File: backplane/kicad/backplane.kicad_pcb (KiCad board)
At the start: 4 copper layers, 141.2 x 81.1 mm, 6 parts, among them J1 weactstm32h7xx, J2 pcie_98, J3 pcie_98, J4 pcie_98, J5 pcie_98, J6 pcie_98

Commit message: Work in progress. Backlane kicad.
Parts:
- added H1: MountingHole, MountingHole:MountingHole_3.2mm_M3_Pad_Via, F.Cu at (84.0, 74.0)
- added H2: MountingHole, MountingHole:MountingHole_3.2mm_M3_Pad_Via, F.Cu at (145.0, 133.0)
- added H3: MountingHole, MountingHole:MountingHole_3.2mm_M3_Pad_Via, F.Cu at (84.0, 133.0)
- added H4: MountingHole, MountingHole:MountingHole_3.2mm_M3_Pad_Via, F.Cu at (217.0, 74.0)
- added H5: MountingHole, MountingHole:MountingHole_3.2mm_M3_Pad_Via, F.Cu at (145.0, 74.0)
- added H6: MountingHole, MountingHole:MountingHole_3.2mm_M3_Pad_Via, F.Cu at (217.0, 133.0)
- added J2: Conn_01x05_Pin, backplane:JST_XH_B5B-XH-AM_1x05_P2.50mm_Vertical, F.Cu at (84.0, 100.0)
- added S1: pcie_98, backplane:pcie_98_socket, F.Cu at (100.0, 90.0)
- added S7: pcie_98, backplane:pcie_98_socket, F.Cu at (208.0, 90.0)
- J1: value weactstm32h7xx -> Conn_01x02_Pin; footprint main_board:weact_stm32fh750 -> backplane:JST_XH_B2B-XH-AM_1x02_P2.50mm_Vertical
- S2: renamed from J2; footprint main_board:pcie_98_socket -> backplane:pcie_98_socket
- S3: renamed from J3; footprint main_board:pcie_98_socket -> backplane:pcie_98_socket
- S4: renamed from J4; footprint main_board:pcie_98_socket -> backplane:pcie_98_socket
- S5: renamed from J5; footprint main_board:pcie_98_socket -> backplane:pcie_98_socket
- S6: renamed from J6; footprint main_board:pcie_98_socket -> backplane:pcie_98_socket
- moved S6 77.5 mm to (190.0, 90.0)
- moved S5 76.4 mm to (172.0, 90.0)
- moved S4 74.7 mm to (154.0, 90.0)
- moved S3 72.9 mm to (136.0, 90.0)
- moved S2 70.1 mm to (118.0, 90.0)
- moved J1 50.6 mm to (84.0, 87.0), turned to -90 degrees
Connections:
- J1 pad 1: /GND -> unconnected-(J1-Pin_1-Pad1)
- J1 pad 2: /5V -> unconnected-(J1-Pin_2-Pad2)
- S2 pad A1: unconnected-(J2-Pin_a1-PadA1) -> /A1
- S2 pad A10: unconnected-(J2-Pin_a10-PadA10) -> /A10
- S2 pad A11: unconnected-(J2-Pin_A11-PadA11) -> /A11
- S2 pad A12: unconnected-(J2-Pin_a12-PadA12) -> /A12
- S2 pad A13: unconnected-(J2-Pin_a13-PadA13) -> /A13
- S2 pad A14: unconnected-(J2-Pin_a14-PadA14) -> /A14
- S2 pad A15: unconnected-(J2-Pin_a15-PadA15) -> /A15
- S2 pad A16: unconnected-(J2-Pin_a16-PadA16) -> /A16
- S2 pad A17: unconnected-(J2-Pin_a17-PadA17) -> /A17
- S2 pad A18: unconnected-(J2-Pin_a18-PadA18) -> /A18
- S2 pad A19: unconnected-(J2-Pin_a19-PadA19) -> /A19
- S2 pad A2: unconnected-(J2-Pin_a2-PadA2) -> /A2
- S2 pad A21: unconnected-(J2-Pin_a21-PadA21) -> /A21
- S2 pad A22: unconnected-(J2-Pin_a22-PadA22) -> /A22
- S2 pad A23: unconnected-(J2-Pin_a23-PadA23) -> /A23
- S2 pad A24: unconnected-(J2-Pin_a24-PadA24) -> /A24
- S2 pad A25: unconnected-(J2-Pin_a25-PadA25) -> /A25
- S2 pad A26: unconnected-(J2-Pin_a26-PadA26) -> /A26
- S2 pad A27: unconnected-(J2-Pin_a27-PadA27) -> /A27
- S2 pad A28: unconnected-(J2-Pin_a28-PadA28) -> /A28
- S2 pad A29: unconnected-(J2-Pin_a29-PadA29) -> /A29
- S2 pad A3: unconnected-(J2-Pin_a3-PadA3) -> /A3
- S2 pad A30: unconnected-(J2-Pin_a30-PadA30) -> /A30
- S2 pad A31: unconnected-(J2-Pin_a31-PadA31) -> /A31
- S2 pad A32: unconnected-(J2-Pin_a32-PadA32) -> /A32
- S2 pad A33: unconnected-(J2-Pin_a33-PadA33) -> /A33
- S2 pad A34: unconnected-(J2-Pin_a34-PadA34) -> /A34
- S2 pad A35: unconnected-(J2-Pin_a35-PadA35) -> /A35
- S2 pad A36: unconnected-(J2-Pin_a36-PadA36) -> /A36
- S2 pad A37: unconnected-(J2-Pin_a37-PadA37) -> /A37
- S2 pad A38: unconnected-(J2-Pin_a38-PadA38) -> /A38
- S2 pad A39: unconnected-(J2-Pin_a39-PadA39) -> /A39
- S2 pad A4: unconnected-(J2-Pin_a4-PadA4) -> /A4
- S2 pad A40: unconnected-(J2-Pin_a40-PadA40) -> /A40
- S2 pad A41: unconnected-(J2-Pin_a41-PadA41) -> /A41
- S2 pad A42: unconnected-(J2-Pin_a42-PadA42) -> /A42
- S2 pad A43: unconnected-(J2-Pin_a43-PadA43) -> /A43
- S2 pad A44: unconnected-(J2-Pin_a44-PadA44) -> /A44
- S2 pad A45: unconnected-(J2-Pin_a45-PadA45) -> /A45
- S2 pad A46: unconnected-(J2-Pin_a46-PadA46) -> /A46
- S2 pad A47: unconnected-(J2-Pin_a47-PadA47) -> /A47
- S2 pad A48: unconnected-(J2-Pin_a48-PadA48) -> /A48
- S2 pad A49: unconnected-(J2-Pin_a49-PadA49) -> /A49
- S2 pad A5: unconnected-(J2-Pin_a5-PadA5) -> /A5
- S2 pad A6: unconnected-(J2-Pin_a6-PadA6) -> /A6
- S2 pad A7: unconnected-(J2-Pin_a7-PadA7) -> /A7
- S2 pad A8: unconnected-(J2-Pin_a8-PadA8) -> /A8
- S2 pad A9: unconnected-(J2-Pin_a9-PadA9) -> /A9
- S2 pad B1: unconnected-(J2-Pin_b1-PadB1) -> /B1
- S2 pad B10: unconnected-(J2-Pin_b10-PadB10) -> /B10
- S2 pad B11: unconnected-(J2-Pin_b11-PadB11) -> /B11
- S2 pad B12: unconnected-(J2-Pin_b12-PadB12) -> /B12
- S2 pad B13: unconnected-(J2-Pin_b13-PadB13) -> /B13
- S2 pad B14: unconnected-(J2-Pin_b14-PadB14) -> /B14
- S2 pad B15: unconnected-(J2-Pin_b15-PadB15) -> /B15
- S2 pad B16: unconnected-(J2-Pin_b16-PadB16) -> /B16
- S2 pad B17: unconnected-(J2-Pin_b17-PadB17) -> /B17
- S2 pad B18: unconnected-(J2-Pin_b18-PadB18) -> /B18
- S2 pad B19: unconnected-(J2-Pin_b19-PadB19) -> /B19
- S2 pad B2: unconnected-(J2-Pin_b2-PadB2) -> /B2
- S2 pad B20: unconnected-(J2-Pin_b20-PadB20) -> /B20
- S2 pad B21: unconnected-(J2-Pin_b21-PadB21) -> /B21
- S2 pad B22: unconnected-(J2-Pin_b22-PadB22) -> /B22
- S2 pad B23: unconnected-(J2-Pin_b23-PadB23) -> /B23
- S2 pad B3: unconnected-(J2-Pin_b3-PadB3) -> /B3
- S2 pad B4: unconnected-(J2-Pin_b4-PadB4) -> /B4
- S2 pad B5: unconnected-(J2-Pin_b5-PadB5) -> /B5
- S2 pad B6: unconnected-(J2-Pin_b6-PadB6) -> /B6
- S2 pad B7: unconnected-(J2-Pin_b7-PadB7) -> /B7
- S2 pad B8: unconnected-(J2-Pin_b8-PadB8) -> /B8
- S2 pad B9: unconnected-(J2-Pin_b9-PadB9) -> /B9
- S3 pad A1: unconnected-(J3-Pin_a1-PadA1) -> /A1
- S3 pad A10: unconnected-(J3-Pin_a10-PadA10) -> /A10
- S3 pad A11: unconnected-(J3-Pin_A11-PadA11) -> /A11
- S3 pad A12: unconnected-(J3-Pin_a12-PadA12) -> /A12
- S3 pad A13: unconnected-(J3-Pin_a13-PadA13) -> /A13
- S3 pad A14: unconnected-(J3-Pin_a14-PadA14) -> /A14
- S3 pad A15: unconnected-(J3-Pin_a15-PadA15) -> /A15
- S3 pad A16: unconnected-(J3-Pin_a16-PadA16) -> /A16
- S3 pad A17: unconnected-(J3-Pin_a17-PadA17) -> /A17
- S3 pad A18: unconnected-(J3-Pin_a18-PadA18) -> /A18
- S3 pad A19: unconnected-(J3-Pin_a19-PadA19) -> /A19
- S3 pad A2: unconnected-(J3-Pin_a2-PadA2) -> /A2
- S3 pad A21: unconnected-(J3-Pin_a21-PadA21) -> /A21
- S3 pad A22: unconnected-(J3-Pin_a22-PadA22) -> /A22
- S3 pad A23: unconnected-(J3-Pin_a23-PadA23) -> /A23
- S3 pad A24: unconnected-(J3-Pin_a24-PadA24) -> /A24
- S3 pad A25: unconnected-(J3-Pin_a25-PadA25) -> /A25
- S3 pad A26: unconnected-(J3-Pin_a26-PadA26) -> /A26
- S3 pad A27: unconnected-(J3-Pin_a27-PadA27) -> /A27
- S3 pad A28: unconnected-(J3-Pin_a28-PadA28) -> /A28
- S3 pad A29: unconnected-(J3-Pin_a29-PadA29) -> /A29
- S3 pad A3: unconnected-(J3-Pin_a3-PadA3) -> /A3
- S3 pad A30: unconnected-(J3-Pin_a30-PadA30) -> /A30
- S3 pad A31: unconnected-(J3-Pin_a31-PadA31) -> /A31
- S3 pad A32: unconnected-(J3-Pin_a32-PadA32) -> /A32
- S3 pad A33: unconnected-(J3-Pin_a33-PadA33) -> /A33
- S3 pad A34: unconnected-(J3-Pin_a34-PadA34) -> /A34
- S3 pad A35: unconnected-(J3-Pin_a35-PadA35) -> /A35
- S3 pad A36: unconnected-(J3-Pin_a36-PadA36) -> /A36
- S3 pad A37: unconnected-(J3-Pin_a37-PadA37) -> /A37
- S3 pad A38: unconnected-(J3-Pin_a38-PadA38) -> /A38
- S3 pad A39: unconnected-(J3-Pin_a39-PadA39) -> /A39
- S3 pad A4: unconnected-(J3-Pin_a4-PadA4) -> /A4
- S3 pad A40: unconnected-(J3-Pin_a40-PadA40) -> /A40
- S3 pad A41: unconnected-(J3-Pin_a41-PadA41) -> /A41
- S3 pad A42: unconnected-(J3-Pin_a42-PadA42) -> /A42
- S3 pad A43: unconnected-(J3-Pin_a43-PadA43) -> /A43
- S3 pad A44: unconnected-(J3-Pin_a44-PadA44) -> /A44
- S3 pad A45: unconnected-(J3-Pin_a45-PadA45) -> /A45
- S3 pad A46: unconnected-(J3-Pin_a46-PadA46) -> /A46
- S3 pad A47: unconnected-(J3-Pin_a47-PadA47) -> /A47
- S3 pad A48: unconnected-(J3-Pin_a48-PadA48) -> /A48
- S3 pad A49: unconnected-(J3-Pin_a49-PadA49) -> /A49
- S3 pad A5: unconnected-(J3-Pin_a5-PadA5) -> /A5
- S3 pad A6: unconnected-(J3-Pin_a6-PadA6) -> /A6
- S3 pad A7: unconnected-(J3-Pin_a7-PadA7) -> /A7
- S3 pad A8: unconnected-(J3-Pin_a8-PadA8) -> /A8
- S3 pad A9: unconnected-(J3-Pin_a9-PadA9) -> /A9
- S3 pad B1: unconnected-(J3-Pin_b1-PadB1) -> /B1
- S3 pad B10: unconnected-(J3-Pin_b10-PadB10) -> /B10
- S3 pad B11: unconnected-(J3-Pin_b11-PadB11) -> /B11
- S3 pad B12: unconnected-(J3-Pin_b12-PadB12) -> /B12
- S3 pad B13: unconnected-(J3-Pin_b13-PadB13) -> /B13
- S3 pad B14: unconnected-(J3-Pin_b14-PadB14) -> /B14
- S3 pad B15: unconnected-(J3-Pin_b15-PadB15) -> /B15
- S3 pad B16: unconnected-(J3-Pin_b16-PadB16) -> /B16
- S3 pad B17: unconnected-(J3-Pin_b17-PadB17) -> /B17
- S3 pad B18: unconnected-(J3-Pin_b18-PadB18) -> /B18
- S3 pad B19: unconnected-(J3-Pin_b19-PadB19) -> /B19
- S3 pad B2: unconnected-(J3-Pin_b2-PadB2) -> /B2
- S3 pad B20: unconnected-(J3-Pin_b20-PadB20) -> /B20
- S3 pad B21: unconnected-(J3-Pin_b21-PadB21) -> /B21
- S3 pad B22: unconnected-(J3-Pin_b22-PadB22) -> /B22
- S3 pad B23: unconnected-(J3-Pin_b23-PadB23) -> /B23
- S3 pad B3: unconnected-(J3-Pin_b3-PadB3) -> /B3
- S3 pad B4: unconnected-(J3-Pin_b4-PadB4) -> /B4
- S3 pad B5: unconnected-(J3-Pin_b5-PadB5) -> /B5
- S3 pad B6: unconnected-(J3-Pin_b6-PadB6) -> /B6
- S3 pad B7: unconnected-(J3-Pin_b7-PadB7) -> /B7
- S3 pad B8: unconnected-(J3-Pin_b8-PadB8) -> /B8
- S3 pad B9: unconnected-(J3-Pin_b9-PadB9) -> /B9
- S4 pad A1: unconnected-(J4-Pin_a1-PadA1) -> /A1
- S4 pad A10: unconnected-(J4-Pin_a10-PadA10) -> /A10
- S4 pad A11: unconnected-(J4-Pin_A11-PadA11) -> /A11
- S4 pad A12: unconnected-(J4-Pin_a12-PadA12) -> /A12
- S4 pad A13: unconnected-(J4-Pin_a13-PadA13) -> /A13
- S4 pad A14: unconnected-(J4-Pin_a14-PadA14) -> /A14
- S4 pad A15: unconnected-(J4-Pin_a15-PadA15) -> /A15
- S4 pad A16: unconnected-(J4-Pin_a16-PadA16) -> /A16
- S4 pad A17: unconnected-(J4-Pin_a17-PadA17) -> /A17
- S4 pad A18: unconnected-(J4-Pin_a18-PadA18) -> /A18
- S4 pad A19: unconnected-(J4-Pin_a19-PadA19) -> /A19
- S4 pad A2: unconnected-(J4-Pin_a2-PadA2) -> /A2
- S4 pad A21: unconnected-(J4-Pin_a21-PadA21) -> /A21
- S4 pad A22: unconnected-(J4-Pin_a22-PadA22) -> /A22
- S4 pad A23: unconnected-(J4-Pin_a23-PadA23) -> /A23
- S4 pad A24: unconnected-(J4-Pin_a24-PadA24) -> /A24
- S4 pad A25: unconnected-(J4-Pin_a25-PadA25) -> /A25
- S4 pad A26: unconnected-(J4-Pin_a26-PadA26) -> /A26
- S4 pad A27: unconnected-(J4-Pin_a27-PadA27) -> /A27
- S4 pad A28: unconnected-(J4-Pin_a28-PadA28) -> /A28
- S4 pad A29: unconnected-(J4-Pin_a29-PadA29) -> /A29
- S4 pad A3: unconnected-(J4-Pin_a3-PadA3) -> /A3
- S4 pad A30: unconnected-(J4-Pin_a30-PadA30) -> /A30
- S4 pad A31: unconnected-(J4-Pin_a31-PadA31) -> /A31
- S4 pad A32: unconnected-(J4-Pin_a32-PadA32) -> /A32
- S4 pad A33: unconnected-(J4-Pin_a33-PadA33) -> /A33
- S4 pad A34: unconnected-(J4-Pin_a34-PadA34) -> /A34
- S4 pad A35: unconnected-(J4-Pin_a35-PadA35) -> /A35
- S4 pad A36: unconnected-(J4-Pin_a36-PadA36) -> /A36
- S4 pad A37: unconnected-(J4-Pin_a37-PadA37) -> /A37
- S4 pad A38: unconnected-(J4-Pin_a38-PadA38) -> /A38
- S4 pad A39: unconnected-(J4-Pin_a39-PadA39) -> /A39
- S4 pad A4: unconnected-(J4-Pin_a4-PadA4) -> /A4
- S4 pad A40: unconnected-(J4-Pin_a40-PadA40) -> /A40
- S4 pad A41: unconnected-(J4-Pin_a41-PadA41) -> /A41
- S4 pad A42: unconnected-(J4-Pin_a42-PadA42) -> /A42
- S4 pad A43: unconnected-(J4-Pin_a43-PadA43) -> /A43
- S4 pad A44: unconnected-(J4-Pin_a44-PadA44) -> /A44
- S4 pad A45: unconnected-(J4-Pin_a45-PadA45) -> /A45
- S4 pad A46: unconnected-(J4-Pin_a46-PadA46) -> /A46
- S4 pad A47: unconnected-(J4-Pin_a47-PadA47) -> /A47
- S4 pad A48: unconnected-(J4-Pin_a48-PadA48) -> /A48
- S4 pad A49: unconnected-(J4-Pin_a49-PadA49) -> /A49
- S4 pad A5: unconnected-(J4-Pin_a5-PadA5) -> /A5
- S4 pad A6: unconnected-(J4-Pin_a6-PadA6) -> /A6
- S4 pad A7: unconnected-(J4-Pin_a7-PadA7) -> /A7
- S4 pad A8: unconnected-(J4-Pin_a8-PadA8) -> /A8
- S4 pad A9: unconnected-(J4-Pin_a9-PadA9) -> /A9
- S4 pad B1: unconnected-(J4-Pin_b1-PadB1) -> /B1
- S4 pad B10: unconnected-(J4-Pin_b10-PadB10) -> /B10
- S4 pad B11: unconnected-(J4-Pin_b11-PadB11) -> /B11
- S4 pad B12: unconnected-(J4-Pin_b12-PadB12) -> /B12
- S4 pad B13: unconnected-(J4-Pin_b13-PadB13) -> /B13
- S4 pad B14: unconnected-(J4-Pin_b14-PadB14) -> /B14
- S4 pad B15: unconnected-(J4-Pin_b15-PadB15) -> /B15
- S4 pad B16: unconnected-(J4-Pin_b16-PadB16) -> /B16
- S4 pad B17: unconnected-(J4-Pin_b17-PadB17) -> /B17
- S4 pad B18: unconnected-(J4-Pin_b18-PadB18) -> /B18
- S4 pad B19: unconnected-(J4-Pin_b19-PadB19) -> /B19
- S4 pad B2: unconnected-(J4-Pin_b2-PadB2) -> /B2
- S4 pad B20: unconnected-(J4-Pin_b20-PadB20) -> /B20
- S4 pad B21: unconnected-(J4-Pin_b21-PadB21) -> /B21
- S4 pad B22: unconnected-(J4-Pin_b22-PadB22) -> /B22
- S4 pad B23: unconnected-(J4-Pin_b23-PadB23) -> /B23
- S4 pad B3: unconnected-(J4-Pin_b3-PadB3) -> /B3
- S4 pad B4: unconnected-(J4-Pin_b4-PadB4) -> /B4
- S4 pad B5: unconnected-(J4-Pin_b5-PadB5) -> /B5
- S4 pad B6: unconnected-(J4-Pin_b6-PadB6) -> /B6
- S4 pad B7: unconnected-(J4-Pin_b7-PadB7) -> /B7
- S4 pad B8: unconnected-(J4-Pin_b8-PadB8) -> /B8
- S4 pad B9: unconnected-(J4-Pin_b9-PadB9) -> /B9
- S5 pad A12: unconnected-(J5-Pin_a12-PadA12) -> /A12
- S5 pad A13: unconnected-(J5-Pin_a13-PadA13) -> /A13
- S5 pad A14: unconnected-(J5-Pin_a14-PadA14) -> /A14
- S5 pad A15: unconnected-(J5-Pin_a15-PadA15) -> /A15
- S5 pad A16: unconnected-(J5-Pin_a16-PadA16) -> /A16
- S5 pad A17: unconnected-(J5-Pin_a17-PadA17) -> /A17
- S5 pad A18: unconnected-(J5-Pin_a18-PadA18) -> /A18
- S5 pad A19: unconnected-(J5-Pin_a19-PadA19) -> /A19
- S5 pad A21: unconnected-(J5-Pin_a21-PadA21) -> /A21
- S5 pad A22: unconnected-(J5-Pin_a22-PadA22) -> /A22
- S5 pad A23: unconnected-(J5-Pin_a23-PadA23) -> /A23
- S5 pad A24: unconnected-(J5-Pin_a24-PadA24) -> /A24
- S5 pad A25: unconnected-(J5-Pin_a25-PadA25) -> /A25
- S5 pad A26: unconnected-(J5-Pin_a26-PadA26) -> /A26
- S5 pad A27: unconnected-(J5-Pin_a27-PadA27) -> /A27
- S5 pad A28: unconnected-(J5-Pin_a28-PadA28) -> /A28
- S5 pad A29: unconnected-(J5-Pin_a29-PadA29) -> /A29
- S5 pad A30: unconnected-(J5-Pin_a30-PadA30) -> /A30
- S5 pad A31: unconnected-(J5-Pin_a31-PadA31) -> /A31
- S5 pad A32: unconnected-(J5-Pin_a32-PadA32) -> /A32
- S5 pad A33: unconnected-(J5-Pin_a33-PadA33) -> /A33
- S5 pad A34: unconnected-(J5-Pin_a34-PadA34) -> /A34
- S5 pad A35: unconnected-(J5-Pin_a35-PadA35) -> /A35
- S5 pad A36: unconnected-(J5-Pin_a36-PadA36) -> /A36
- S5 pad A37: unconnected-(J5-Pin_a37-PadA37) -> /A37
- S5 pad A38: unconnected-(J5-Pin_a38-PadA38) -> /A38
- S5 pad A39: unconnected-(J5-Pin_a39-PadA39) -> /A39
- S5 pad A40: unconnected-(J5-Pin_a40-PadA40) -> /A40
- S5 pad A41: unconnected-(J5-Pin_a41-PadA41) -> /A41
- S5 pad A42: unconnected-(J5-Pin_a42-PadA42) -> /A42
- S5 pad A43: unconnected-(J5-Pin_a43-PadA43) -> /A43
- S5 pad A44: unconnected-(J5-Pin_a44-PadA44) -> /A44
- S5 pad A45: unconnected-(J5-Pin_a45-PadA45) -> /A45
- S5 pad A46: unconnected-(J5-Pin_a46-PadA46) -> /A46
- S5 pad A47: unconnected-(J5-Pin_a47-PadA47) -> /A47
- S5 pad A48: unconnected-(J5-Pin_a48-PadA48) -> /A48
- S5 pad A49: unconnected-(J5-Pin_a49-PadA49) -> /A49
- S5 pad B12: unconnected-(J5-Pin_b12-PadB12) -> /B12
- S5 pad B13: unconnected-(J5-Pin_b13-PadB13) -> /B13
- S5 pad B14: unconnected-(J5-Pin_b14-PadB14) -> /B14
- S5 pad B15: unconnected-(J5-Pin_b15-PadB15) -> /B15
- S5 pad B16: unconnected-(J5-Pin_b16-PadB16) -> /B16
- S5 pad B17: unconnected-(J5-Pin_b17-PadB17) -> /B17
- S5 pad B18: unconnected-(J5-Pin_b18-PadB18) -> /B18
- S5 pad B19: unconnected-(J5-Pin_b19-PadB19) -> /B19
- S5 pad B20: unconnected-(J5-Pin_b20-PadB20) -> /B20
- S5 pad B21: unconnected-(J5-Pin_b21-PadB21) -> /B21
- S5 pad B22: unconnected-(J5-Pin_b22-PadB22) -> /B22
- S5 pad B23: unconnected-(J5-Pin_b23-PadB23) -> /B23
- S6 pad A12: unconnected-(J6-Pin_a12-PadA12) -> /A12
- S6 pad A13: unconnected-(J6-Pin_a13-PadA13) -> /A13
- S6 pad A14: unconnected-(J6-Pin_a14-PadA14) -> /A14
- S6 pad A15: unconnected-(J6-Pin_a15-PadA15) -> /A15
- S6 pad A16: unconnected-(J6-Pin_a16-PadA16) -> /A16
- S6 pad A17: unconnected-(J6-Pin_a17-PadA17) -> /A17
- S6 pad A18: unconnected-(J6-Pin_a18-PadA18) -> /A18
- S6 pad A19: unconnected-(J6-Pin_a19-PadA19) -> /A19
- S6 pad A21: unconnected-(J6-Pin_a21-PadA21) -> /A21
- S6 pad A22: unconnected-(J6-Pin_a22-PadA22) -> /A22
- S6 pad A23: unconnected-(J6-Pin_a23-PadA23) -> /A23
- S6 pad A24: unconnected-(J6-Pin_a24-PadA24) -> /A24
- S6 pad A25: unconnected-(J6-Pin_a25-PadA25) -> /A25
- S6 pad A26: unconnected-(J6-Pin_a26-PadA26) -> /A26
- S6 pad A27: unconnected-(J6-Pin_a27-PadA27) -> /A27
- S6 pad A28: unconnected-(J6-Pin_a28-PadA28) -> /A28
- S6 pad A29: unconnected-(J6-Pin_a29-PadA29) -> /A29
- S6 pad A30: unconnected-(J6-Pin_a30-PadA30) -> /A30
- S6 pad A31: unconnected-(J6-Pin_a31-PadA31) -> /A31
- S6 pad A32: unconnected-(J6-Pin_a32-PadA32) -> /A32
- S6 pad A33: unconnected-(J6-Pin_a33-PadA33) -> /A33
- S6 pad A34: unconnected-(J6-Pin_a34-PadA34) -> /A34
- S6 pad A35: unconnected-(J6-Pin_a35-PadA35) -> /A35
- S6 pad A36: unconnected-(J6-Pin_a36-PadA36) -> /A36
- S6 pad A37: unconnected-(J6-Pin_a37-PadA37) -> /A37
- S6 pad A38: unconnected-(J6-Pin_a38-PadA38) -> /A38
- S6 pad A39: unconnected-(J6-Pin_a39-PadA39) -> /A39
- S6 pad A40: unconnected-(J6-Pin_a40-PadA40) -> /A40
- S6 pad A41: unconnected-(J6-Pin_a41-PadA41) -> /A41
- S6 pad A42: unconnected-(J6-Pin_a42-PadA42) -> /A42
- S6 pad A43: unconnected-(J6-Pin_a43-PadA43) -> /A43
- S6 pad A44: unconnected-(J6-Pin_a44-PadA44) -> /A44
- S6 pad A45: unconnected-(J6-Pin_a45-PadA45) -> /A45
- S6 pad A46: unconnected-(J6-Pin_a46-PadA46) -> /A46
- S6 pad A47: unconnected-(J6-Pin_a47-PadA47) -> /A47
- S6 pad A48: unconnected-(J6-Pin_a48-PadA48) -> /A48
- S6 pad A49: unconnected-(J6-Pin_a49-PadA49) -> /A49
- S6 pad B12: unconnected-(J6-Pin_b12-PadB12) -> /B12
- S6 pad B13: unconnected-(J6-Pin_b13-PadB13) -> /B13
- S6 pad B14: unconnected-(J6-Pin_b14-PadB14) -> /B14
- S6 pad B15: unconnected-(J6-Pin_b15-PadB15) -> /B15
- S6 pad B16: unconnected-(J6-Pin_b16-PadB16) -> /B16
- S6 pad B17: unconnected-(J6-Pin_b17-PadB17) -> /B17
- S6 pad B18: unconnected-(J6-Pin_b18-PadB18) -> /B18
- S6 pad B19: unconnected-(J6-Pin_b19-PadB19) -> /B19
- S6 pad B20: unconnected-(J6-Pin_b20-PadB20) -> /B20
- S6 pad B21: unconnected-(J6-Pin_b21-PadB21) -> /B21
- S6 pad B22: unconnected-(J6-Pin_b22-PadB22) -> /B22
- S6 pad B23: unconnected-(J6-Pin_b23-PadB23) -> /B23
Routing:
- net /A3: track 22.7 -> 0.00 mm
- net /B2: track 18.1 -> 0.00 mm
- net /B4: track 17.8 -> 0.00 mm
- net /B3: track 17.6 -> 0.00 mm
- net /A8: track 17.6 -> 0.00 mm
- net /A2: track 17.5 -> 0.00 mm
- net /A6: track 17.5 -> 0.00 mm
- net /A10: track 17.4 -> 0.00 mm
- net /A4: track 17.4 -> 0.00 mm
- net /B8: track 16.9 -> 0.00 mm
- net /B11: track 16.8 -> 0.00 mm
- net /B9: track 16.7 -> 0.00 mm
- net /B7: track 16.7 -> 0.00 mm
- net /B5: track 16.7 -> 0.00 mm
- net /B1: track 16.7 -> 0.00 mm
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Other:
- board size 141.2 x 81.1 mm -> 141 x 67 mm

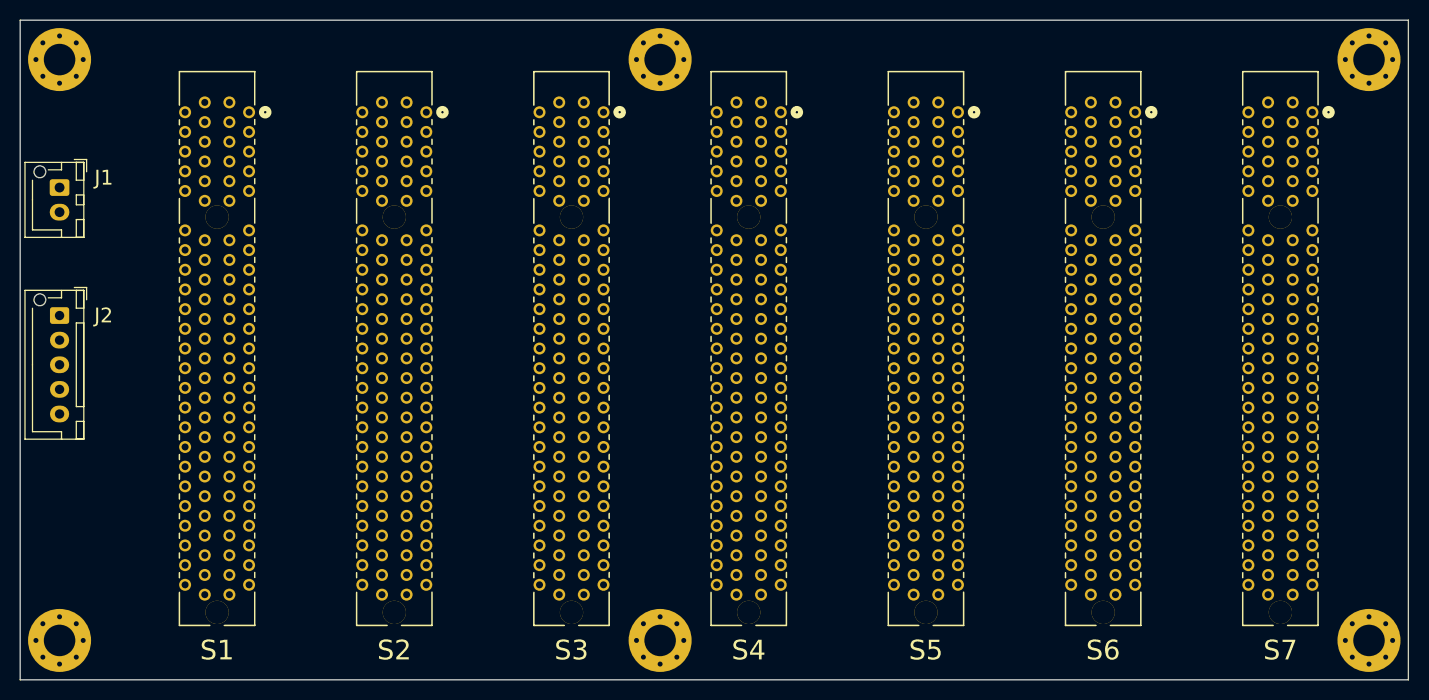
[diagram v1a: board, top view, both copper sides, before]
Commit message: Performed sample bus routing.
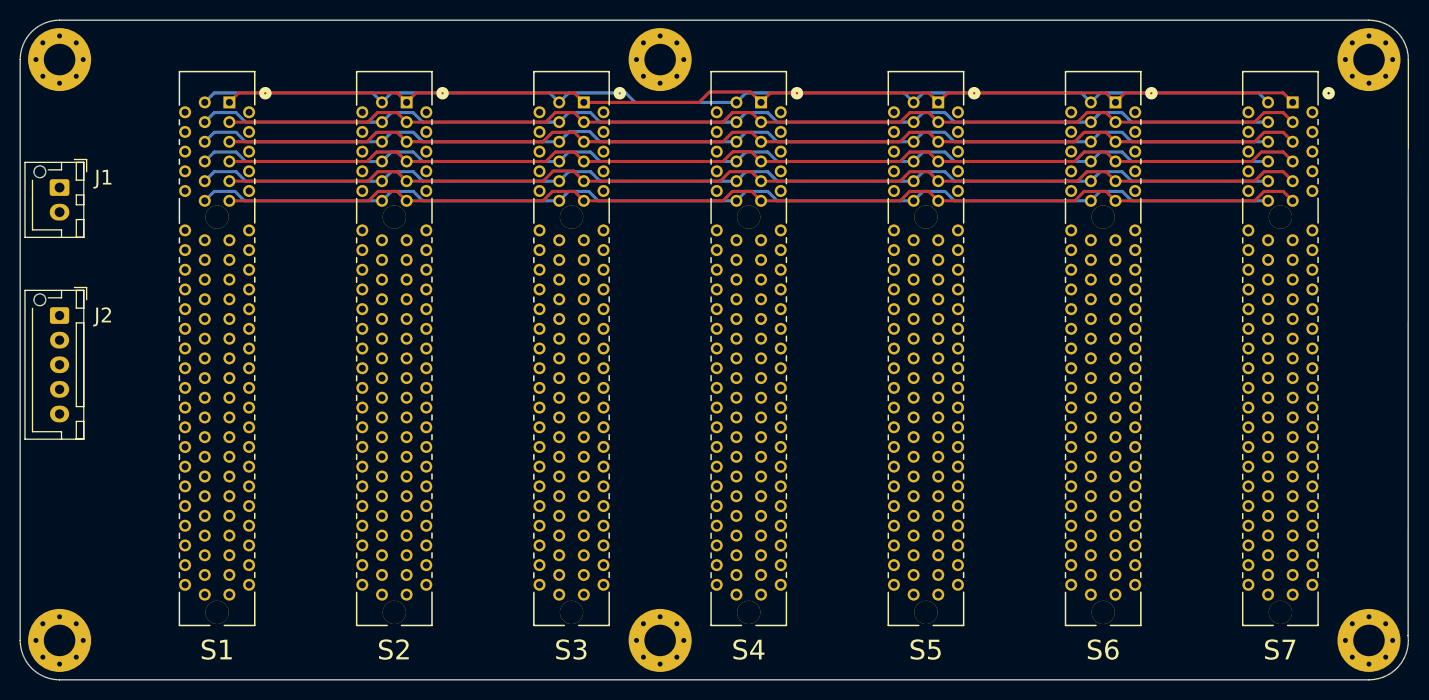
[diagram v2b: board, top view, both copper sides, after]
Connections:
- S2 pad A20: (no net) -> /A20
- S3 pad A20: (no net) -> /A20
- S4 pad A20: (no net) -> /A20
- S5 pad A20: (no net) -> /A20
- S6 pad A20: (no net) -> /A20
- S7 pad A20: (no net) -> /A20
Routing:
- net /B2: track 0.00 -> 120.8 mm
- net /A8: track 0.00 -> 112.9 mm
- net /B4: track 0.00 -> 112.9 mm
- net /B10: track 0.00 -> 112.9 mm
- net /A1: track 0.00 -> 112.9 mm
- net /A6: track 0.00 -> 112.8 mm
- net /B5: track 0.00 -> 112.8 mm
- net /B6: track 0.00 -> 112.8 mm
- net /A9: track 0.00 -> 112.8 mm
- net /B8: track 0.00 -> 112.8 mm
- net /A7: track 0.00 -> 112.8 mm
- net /B11: track 0.00 -> 112.8 mm
- net /B9: track 0.00 -> 112.8 mm
- net /A4: track 0.00 -> 112.8 mm
- net /A11: track 0.00 -> 112.8 mm
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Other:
- outline, holes or cut-outs redrawn

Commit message: Tweaked backplane dimensions.
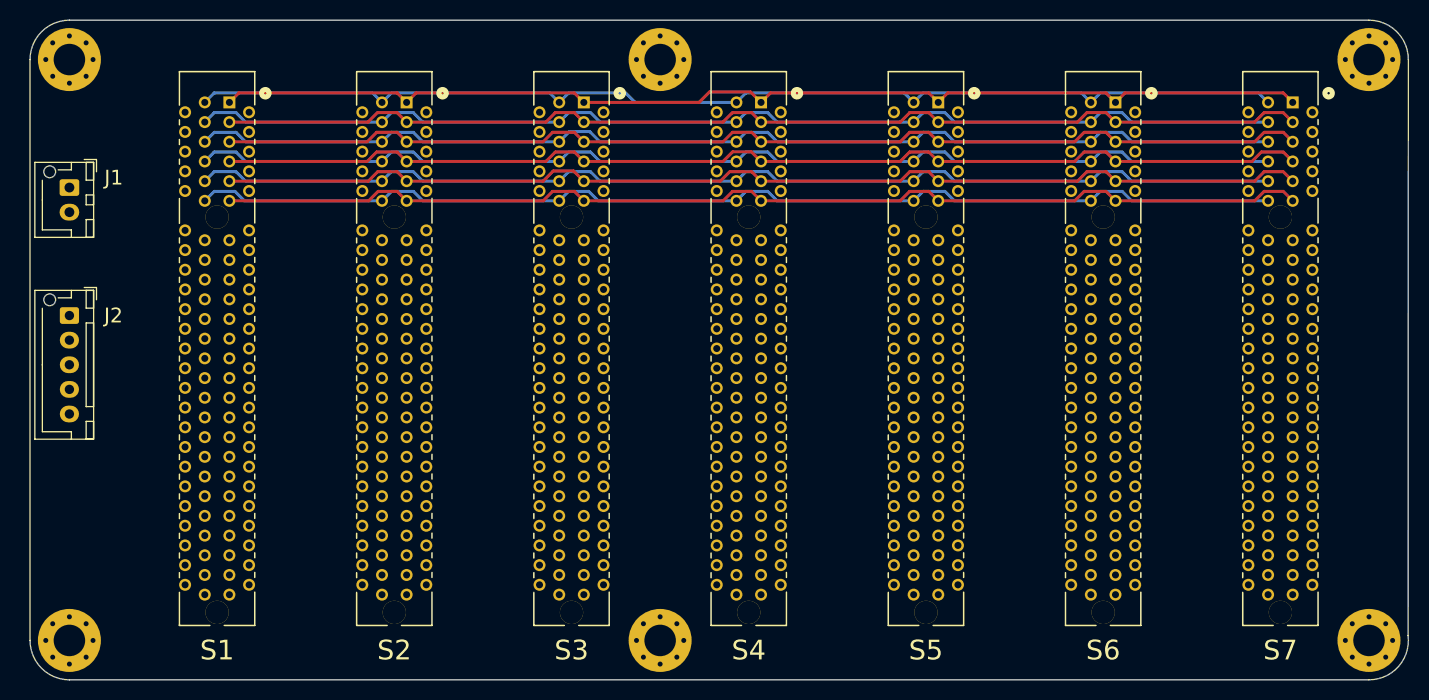
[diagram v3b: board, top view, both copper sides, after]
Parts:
- moved H1 1.00 mm to (85.0, 74.0)
- moved H3 1.00 mm to (85.0, 133.0)
- moved J1 1.00 mm to (85.0, 87.0)
- moved J2 1.00 mm to (85.0, 100.0)
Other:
- board size 141 x 67 mm -> 140 x 67 mm
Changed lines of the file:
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@@
   )
   (footprint "MountingHole:MountingHole_3.2mm_M3_Pad_Via" (layer "F.Cu")
-    (at 84 133)
+    (at 85 133)
     (descr "Mounting Hole 3.2mm, M3")
     (tags "mounting hole 3.2mm m3")
@@
   )
   (footprint "backplane:JST_XH_B2B-XH-AM_1x02_P2.50mm_Vertical" (layer "F.Cu")
-    (at 84 87 -90)
+    (at 85 87 -90)
     (descr "JST XH series connector, B2B-XH-AM, with boss (http://www.jst-mfg.com/product/pdf/eng/eXH.pdf), generated with kicad-footprint-generator")
     (tags "connector JST XH vertical boss")
@@
   )
   (footprint "MountingHole:MountingHole_3.2mm_M3_Pad_Via" (layer "F.Cu")
-    (at 84 74)
+    (at 85 74)
     (descr "Mounting Hole 3.2mm, M3")
     (tags "mounting hole 3.2mm m3")
@@
   )
   (footprint "backplane:JST_XH_B5B-XH-AM_1x05_P2.50mm_Vertical" (layer "F.Cu")
-    (at 84 100 -90)
+    (at 85 100 -90)
     (descr "JST XH series connector, B5B-XH-AM, with boss (http://www.jst-mfg.com/product/pdf/eng/eXH.pdf), generated with kicad-footprint-generator")
     (tags "connector JST XH vertical boss")
@@
     )
   )
-  (gr_line (start 84 137) (end 217 137)
-    (stroke (width 0.1) (type default)) (layer "Edge.Cuts"))
-  (gr_line (start 80 74) (end 80 133)
+  (gr_line (start 85 137) (end 217 137)
     (stroke (width 0.1) (type default)) (layer "Edge.Cuts"))
   (gr_line (start 220.969112 132.503861) (end 221 74)
     (stroke (width 0.1) (type default)) (layer "Edge.Cuts"))
-  (gr_line (start 217 70) (end 84 70)
+  (gr_arc (start 85 137) (mid 82.171573 135.828427) (end 81 133)
     (stroke (width 0.1) (type default)) (layer "Edge.Cuts"))
-  (gr_arc (start 80 74) (mid 81.171573 71.171573) (end 84 70)
+  (gr_line (start 217 70) (end 85 70)
     (stroke (width 0.1) (type default)) (layer "Edge.Cuts"))
-  (gr_arc (start 84 137) (mid 81.171573 135.828427) (end 80 133)
+  (gr_line (start 81 74) (end 81 133)
     (stroke (width 0.1) (type default)) (layer "Edge.Cuts"))
   (gr_arc (start 217 70) (mid 219.828427 71.171573) (end 221 74)
@@
   (gr_arc (start 220.969112 132.503861) (mid 219.998713 135.647211) (end 217 137)
     (stroke (width 0.1) (type default)) (layer "Edge.Cuts"))
+  (gr_arc (start 81 74) (mid 82.171573 71.171573) (end 85 70)
+    (stroke (width 0.1) (type default)) (layer "Edge.Cuts"))
   (segment (start 173.25 78.350004) (end 174.212 77.388004) (width 0.3048) (layer "F.Cu") (net 38))

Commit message: outed all the network of the backplan.
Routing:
- net /A49: track 0.00 -> 140.7 mm
- net /A48: track 0.00 -> 139.3 mm
- net /B48: track 0.00 -> 139.1 mm
- net /A26: track 0.00 -> 120.0 mm
- net /A18: track 0.00 -> 119.9 mm
- net /A24: track 0.00 -> 119.3 mm
- net /A28: track 0.00 -> 119.2 mm
- net /B20: track 0.00 -> 119.2 mm
- net /B12: track 0.00 -> 119.2 mm
- net /A32: track 0.00 -> 119.2 mm
- net /A12: track 0.00 -> 119.2 mm
- net /B14: track 0.00 -> 119.1 mm
- net /B42: track 0.00 -> 119.0 mm
- net /B38: track 0.00 -> 119.0 mm
- net /B32: track 0.00 -> 119.0 mm
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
